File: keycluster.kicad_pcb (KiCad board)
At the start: 2 copper layers, 45.1 x 52.6 mm, 0 parts

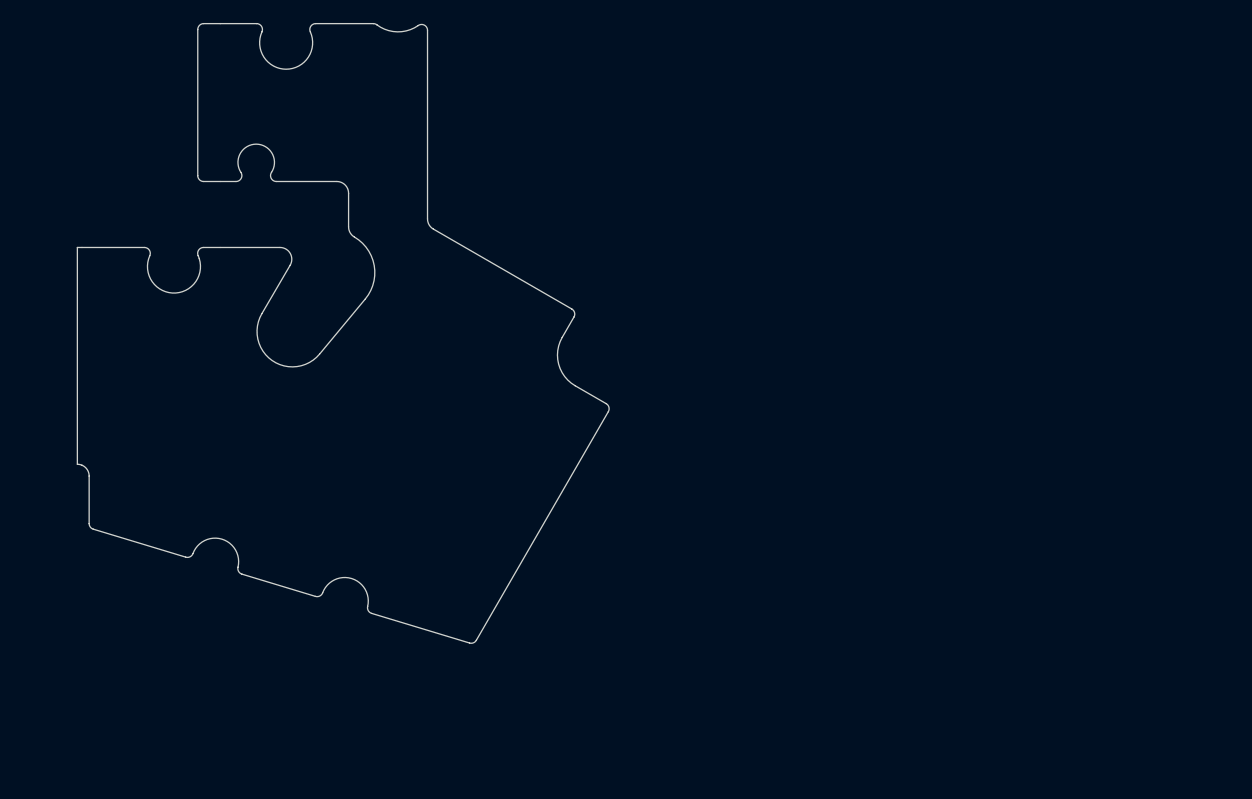
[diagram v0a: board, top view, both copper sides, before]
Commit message: Vertical and trackball pcb.
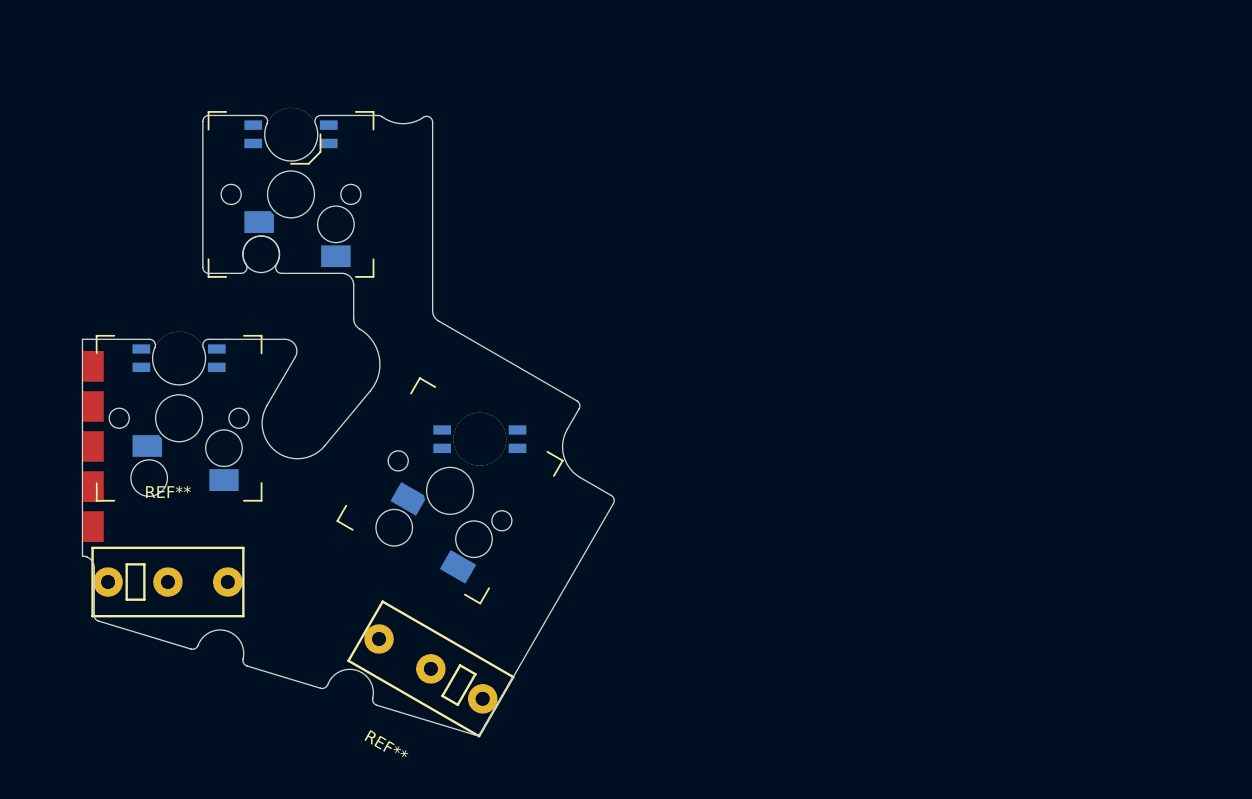
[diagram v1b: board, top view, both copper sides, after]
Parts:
- added REF**: CMI126603D08, ugl:CMI126603D08, F.Cu at (154.6, 128.0)
- added REF**: VAL**, ugl:RGB-LED-D, F.Cu at (158.7, 108.5)
- added REF**: VAL**, ugl:S01_Hybrid_Socket, F.Cu at (142.7, 87.7)
- added REF**: VAL**, ugl:S01_Hybrid_Socket, F.Cu at (133.2, 106.7)
- added REF**: VAL**, ugl:S01_Hybrid_Socket, F.Cu at (156.2, 112.9)
- added REF**: VAL**, ugl:RGB-LED-D, F.Cu at (133.2, 101.6)
- added REF**: VAL**, ugl:RGB_LED, F.Cu at (142.7, 82.6)
- added REF**: CMI126603D08, ugl:CMI126603D08, F.Cu at (132.3, 120.6)
- added REF**: VAL**, ugl:UHK_Connector_TrackBall_Pcb, F.Cu at (123.8, 100.0)

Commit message: Keycluster project files added.
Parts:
- removed REF** (x2): VAL**, ugl:RGB-LED-D
- removed REF** (x3): VAL**, ugl:S01_Hybrid_Socket
- removed REF**: VAL**, ugl:RGB_LED
- added C1: 0.47uF, UGL:SM0603, B.Cu at (154.0, 98.0)
- added C12: 1uF, UGL:SM0603, B.Cu at (138.7, 118.2)
- added C13: 10uF, UGL:SM1206_Diode, B.Cu at (150.8, 96.7)
- added C15: 0.1uF, UGL:SM0603, B.Cu at (157.5, 101.6)
- added C16: 0.47uF, UGL:SM0603, B.Cu at (159.6, 102.4)
- added C17: 0.1uF, UGL:SM0603, B.Cu at (155.5, 106.5)
- added C19: 0.47uF, UGL:SM0603, B.Cu at (153.5, 107.8)
- added C2: 1uF, UGL:SM0603, B.Cu at (138.2, 113.8)
- added C20: 0.1uF, UGL:SM0603, B.Cu at (150.4, 107.7)
- added C3: 0.1uF, UGL:SM0603, B.Cu at (161.0, 120.6)
- added C4: 0.1uF, UGL:SM0603, B.Cu at (141.1, 113.8)
- added C5: 0.1uF, UGL:SM0603, B.Cu at (152.8, 98.0)
- added C7: 0.1uF, UGL:SM0603, B.Cu at (133.7, 113.1)
- added C8: 0.1uF, UGL:SM0603, B.Cu at (135.0, 113.1)
- added D2: LED, UGL:SM0603_Diode, B.Cu at (150.5, 121.5)
- added D_LK1: RGB_LED, UGL:RGB_LED, F.Cu at (133.2, 101.6)
- added D_RK1: RGB_LED, UGL:RGB_LED, F.Cu at (158.7, 108.5)
- added D_TK1: ugl:RGB_LED, UGL:RGB_LED, F.Cu at (142.7, 82.6)
- added FB2: FERRITE_BEAD, UGL:SM0603, B.Cu at (134.5, 115.0)
- added P7: CONN_10, UGL:Tag_Connect_2x5_Header_With_Legs, B.Cu at (143.0, 123.7)
- added P9: CONN_5, FFC_Connector_51281-0594, F.Cu at (144.9, 111.8)
- added R1: 4.7K, UGL:SM0603, B.Cu at (159.8, 123.0)
- added R2: 330, UGL:SM0603, B.Cu at (150.5, 120.1)
- added R20: 100k, UGL:SM0603, B.Cu at (153.6, 110.8)
- added R3: 100K, UGL:SM0603, B.Cu at (149.2, 107.7)
- added R30: 100K, UGL:SM0603, B.Cu at (151.6, 107.7)
- added R6: 47, UGL:SM0603, B.Cu at (134.8, 122.7)
- added R7: 47, UGL:SM0603, B.Cu at (134.8, 118.6)
- added R8: 47K, UGL:SM0603, B.Cu at (157.5, 104.4)
- added SW1: CT05-3050-G1, UGL:Reed_Switch_CT05-3050-G1, B.Cu at (163.3, 122.0)
- added SW_LK1: LK, UGL:S01_Hybrid_Socket, F.Cu at (133.2, 106.7)
- added SW_RK1: RK, UGL:S01_Hybrid_Socket, F.Cu at (156.2, 112.9)
- added SW_TK1: TK, UGL:S01_Hybrid_Socket, F.Cu at (142.7, 87.7)
- added TP_3.3V1: 3.3V, UGL:Test_Point, B.Cu at (210.2, 104.6)
- added TP_5V1: 5V, UGL:Test_Point, B.Cu at (218.3, 101.9)
- added TP_CS1: LED_CS1, UGL:Test_Point, B.Cu at (148.4, 83.4)
- added TP_CS2: LED_CS2, UGL:Test_Point, B.Cu at (136.4, 104.6)
- added TP_CS3: LED_CS3, UGL:Test_Point, B.Cu at (162.0, 111.4)
- added TP_GND1: GND, UGL:Test_Point, B.Cu at (150.8, 93.1)
- added TP_IICRST1: IICRST, UGL:Test_Point, B.Cu at (218.8, 107.2)
- added TP_INTB1: SDA, UGL:Test_Point, B.Cu at (210.6, 106.7)
- added TP_KEY_LEFT1: KEYS_ROW2, UGL:Test_Point, B.Cu at (213.4, 99.9)
- added TP_KEY_MLEFT1: KEYS_ROW4, UGL:Test_Point, B.Cu at (220.0, 107.2)
- added TP_KEY_MRIGHT1: KEYS_ROW5, UGL:Test_Point, B.Cu at (221.7, 102.6)
- added TP_KEY_RIGHT1: KEYS_ROW3, UGL:Test_Point, B.Cu at (219.5, 100.7)
- added TP_KEY_TOP1: KEYS_ROW1, UGL:Test_Point, B.Cu at (213.3, 103.6)
- added TP_RESET1: RESET, UGL:Test_Point, B.Cu at (155.6, 121.3)
- added TP_SCL1: SCL, UGL:Test_Point, B.Cu at (216.4, 106.5)
- added TP_SCL_BOTTOM1: SCL_BOTTOM, UGL:Test_Point, B.Cu at (219.0, 110.1)
- added TP_SDA1: SDA, UGL:Test_Point, B.Cu at (212.6, 105.8)
- added TP_SDA_BOTTOM1: SDA_BOTTOM, UGL:Test_Point, B.Cu at (212.6, 108.2)
- added TP_SDB1: SDB, UGL:Test_Point, B.Cu at (206.8, 102.0)
- added TP_SW1: LED_SW1, UGL:Test_Point, B.Cu at (139.5, 85.8)
- added TP_SW2: LED_SW2, UGL:Test_Point, B.Cu at (137.8, 81.8)
- added TP_SW3: LED_SW3, UGL:Test_Point, B.Cu at (138.7, 100.8)
- added TP_SWDCLK1: SWDCLK, UGL:Test_Point, B.Cu at (207.0, 99.2)
- added TP_SWDIO1: SWDIO, UGL:Test_Point, B.Cu at (208.2, 99.2)
- added TP_TEST_LED1: TEST_LED, UGL:Test_Point, B.Cu at (217.8, 110.1)
- added TP_TEST_LED_R1: TEST_LED_R, UGL:Test_Point, B.Cu at (209.0, 104.6)
- added TP_VCC_BOTTOM1: VCC_BOTTOM, UGL:Test_Point, B.Cu at (210.4, 102.0)
- added U1: MKL03Z32VFK4, UGL:QFN-24-1EP_4x4mm_Pitch0.5mm, B.Cu at (145.0, 113.5)
- added U2: IS31FL3737, UGL:QFN-40_EP_5x5_Pitch0.4mm, B.Cu at (153.6, 102.6)
- added U4: ESD, UGL:SC-74-TVS, B.Cu at (131.0, 115.9)
- added VR1: MIC5504-3.3YM5, UGL:SOT-23-5, B.Cu at (138.2, 115.9)
- added hole 2.2mm: VAL**, UGL:hole_4.0mm, F.Cu at (144.8, 119.1)
- P2: renamed from REF**; value VAL** -> CONN_5
- SW_MLK1: renamed from REF**; value CMI126603D08 -> MLK
- SW_MRK1: renamed from REF**; value CMI126603D08 -> MRK
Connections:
- P2 pad 1: (no net) -> /VCC_BOTTOM
- P2 pad 2: (no net) -> /SDA_BOTTOM
- P2 pad 3: (no net) -> /SCL_BOTTOM
- P2 pad 4: (no net) -> GND
- P2 pad 5: (no net) -> GND
- SW_MLK1 pad 1: (no net) -> /KEY_MLEFT
- SW_MLK1 pad 2: (no net) -> GND
- SW_MRK1 pad 1: (no net) -> /KEY_MRIGHT
- SW_MRK1 pad 2: (no net) -> GND

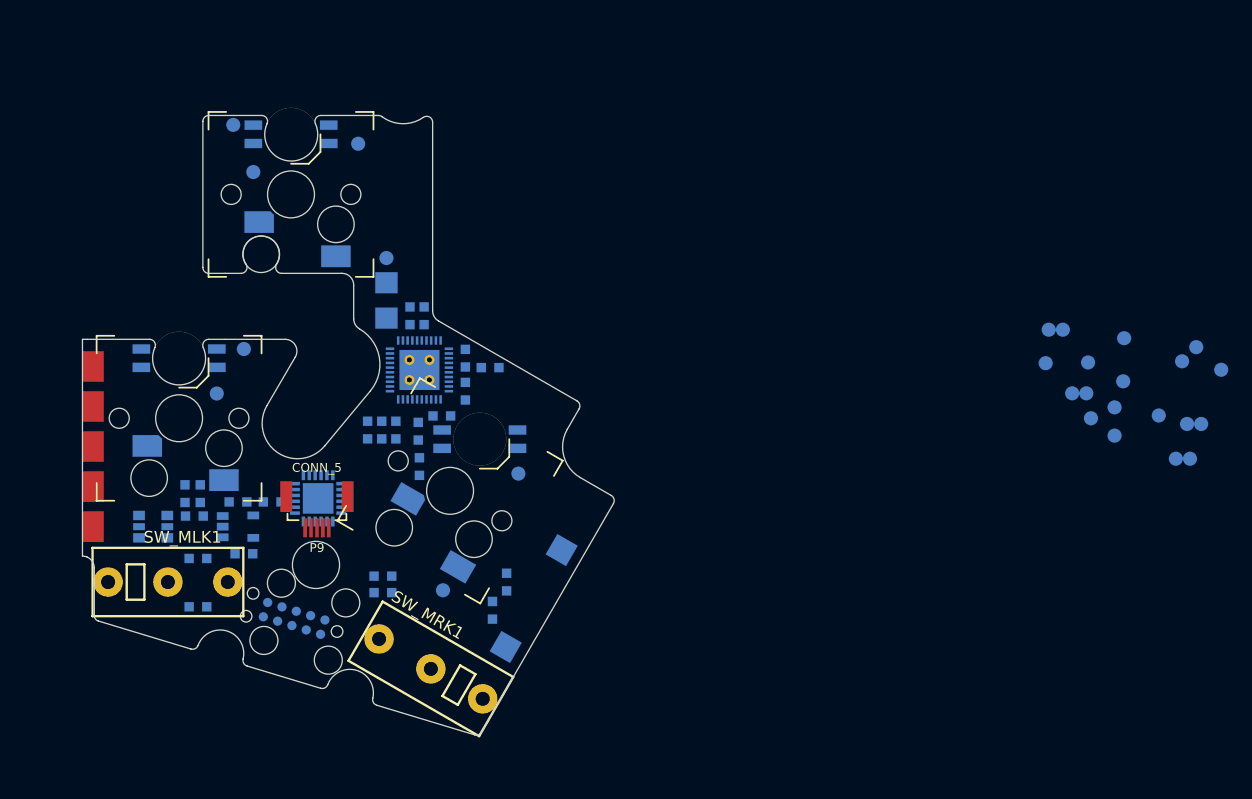
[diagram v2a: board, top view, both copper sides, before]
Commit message: Wiring on main pcb.
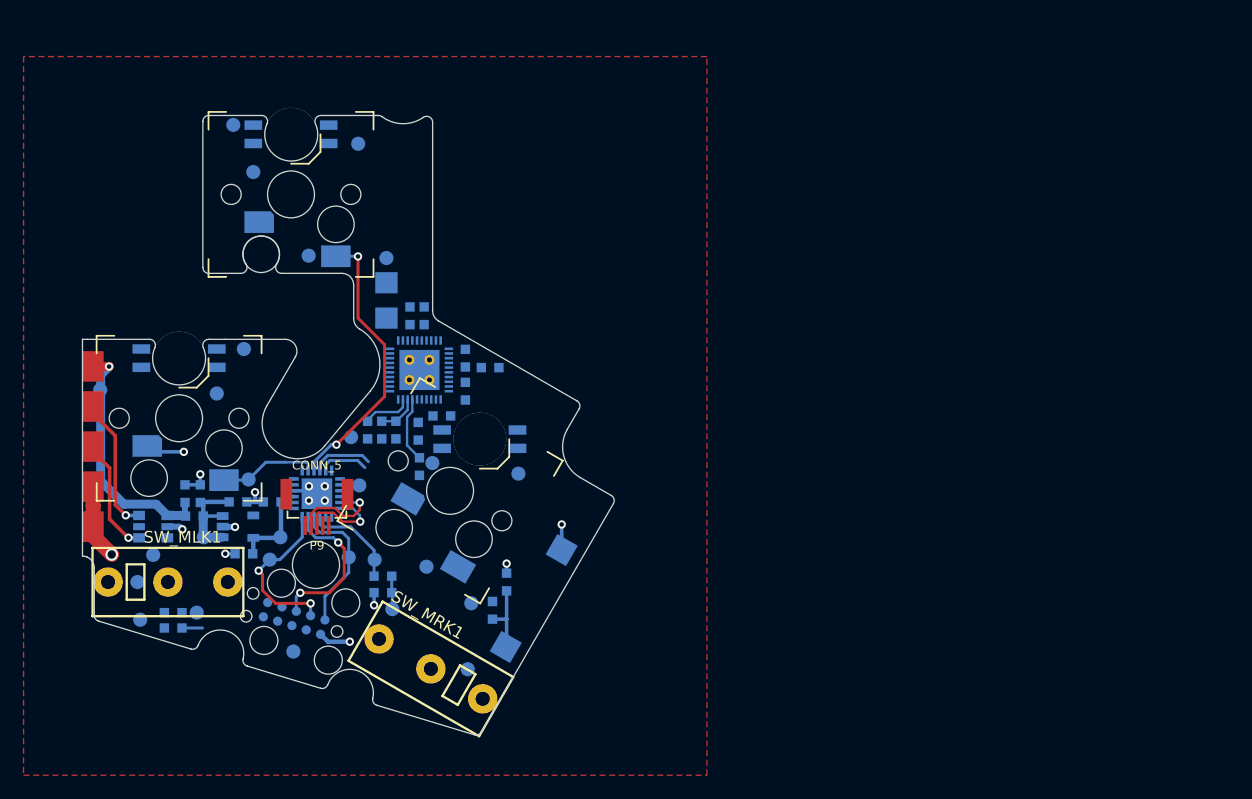
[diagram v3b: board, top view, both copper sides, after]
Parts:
- moved TP_KEY_MLEFT1 91.3 mm to (129.7, 120.6)
- moved TP_SCL_BOTTOM1 90.1 mm to (129.9, 123.8)
- moved TP_5V1 84.4 mm to (135.3, 116.8)
- moved TP_VCC_BOTTOM1 83.9 mm to (126.5, 104.3)
- moved TP_SDA_BOTTOM1 82.2 mm to (131.0, 118.3)
- moved TP_SDA1 79.8 mm to (134.7, 123.2)
- moved TP_SCL1 76.1 mm to (142.9, 126.5)
- moved TP_KEY_LEFT1 75.3 mm to (139.1, 111.9)
- moved TP_IICRST1 70.4 mm to (148.5, 112.4)
- moved TP_SWDIO1 70.1 mm to (140.9, 118.7)
- moved TP_KEY_TOP1 70.0 mm to (144.2, 92.9)
- moved TP_3.3V1 69.5 mm to (141.8, 116.8)
- moved TP_KEY_MRIGHT1 68.8 mm to (157.7, 128.0)
- moved TP_TEST_LED1 68.5 mm to (149.8, 118.7)
- moved TP_KEY_RIGHT1 67.9 mm to (154.2, 119.3)
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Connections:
- U1 pad 10: /KEY_MLEFT -> /KEY_RIGHT
- U1 pad 7: /KEY_TOP -> /KEY_MLEFT
- U1 pad 9: /KEY_RIGHT -> /KEY_TOP
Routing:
- net GND: track 0.00 -> 25.7 mm, vias 0 -> 15
- net /KEY_TOP: track 0.00 -> 23.7 mm, vias 0 -> 2
- net /VCC_BOTTOM: track 0.00 -> 20.9 mm, vias 0 -> 1
- net /RESET: track 0.00 -> 19.3 mm, vias 0 -> 2
- net /SWDIO: track 0.00 -> 14.0 mm, vias 0 -> 2
- net /SWDCLK: track 0.00 -> 11.9 mm
- net /SDA_BOTTOM: track 0.00 -> 11.5 mm, vias 0 -> 1
- net /SCL: track 0.00 -> 10.1 mm, vias 0 -> 1
- net /SCL_BOTTOM: track 0.00 -> 9.90 mm, vias 0 -> 1
- net +5V: track 0.00 -> 8.64 mm
- net /KEY_LEFT: track 0.00 -> 8.39 mm
- net /TEST_LED: track 0.00 -> 8.34 mm
- net +3V3: track 0.00 -> 7.98 mm
- net /ADDR: track 0.00 -> 7.67 mm, vias 0 -> 1
- net /INTB: track 0.00 -> 5.57 mm
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- added copper zone on F.Cu, net GND
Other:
- net class Default: clearance 0.2 -> 0.1778; trace_width 0.25 -> 0.2032; via_dia 0.8 -> 1.0668; via_drill 0.4 -> 0.7112
- rule trace_clearance: 0.2 -> 0.1778
- rule trace_min: 0.2 -> 0.2032
- rule via_min_drill: 0.3 -> 0.381
- rule via_min_size: 0.4 -> 0.7112

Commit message: Wiring on main pcb.
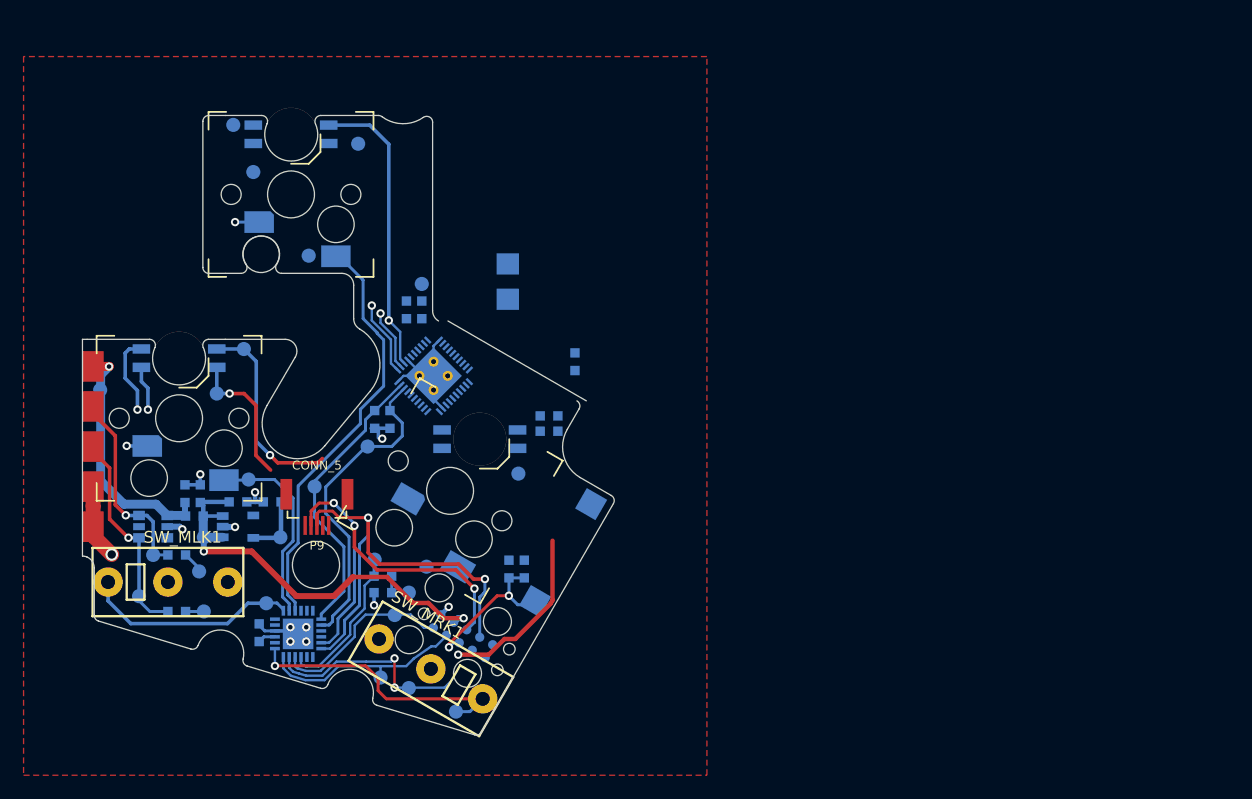
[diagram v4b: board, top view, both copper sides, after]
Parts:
- removed C1: 0.47uF, UGL:SM0603
- removed C20, C5: 0.1uF, UGL:SM0603
- removed R20: 100k, UGL:SM0603
- removed TP_INTB1: SDA, UGL:Test_Point
- moved P7 14.4 mm to (157.3, 125.2), turned to 330 degrees
- moved TP_SWDIO1 13.7 mm to (150.3, 128.7)
- moved U1 12.0 mm to (143.3, 125.0)
- moved C19 11.1 mm to (164.6, 107.8), turned to 0 degrees
- moved TP_KEY_MLEFT1 11.1 mm to (140.6, 122.4)
- moved C13 10.4 mm to (161.1, 95.1)
- moved R8 9.63 mm to (166.8, 101.9)
- moved C17 9.49 mm to (152.5, 97.5), turned to 90 degrees
- moved TP_RESET1 8.94 mm to (152.7, 129.6)
- moved TP_SCL1 8.33 mm to (135.3, 123.1)
- moved C12 6.82 mm to (140.0, 124.9), turned to 270 degrees
- moved C16 6.47 mm to (164.6, 106.5)
- moved TP_SWDCLK1 6.26 mm to (151.5, 123.4)
- moved C15 5.52 mm to (153.8, 97.5)
- moved R6 4.91 mm to (133.0, 118.3)
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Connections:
- U1 pad 1: Net-(U1-Pad1) -> /KEY_MRIGHT
- U1 pad 11: /KEY_MRIGHT -> Net-(U1-Pad11)
- U1 pad 13: /SDB -> /IICRST
- U1 pad 14: /IICRST -> /SDB
- U2 pad 37: /INTB -> Net-(U2-Pad37)
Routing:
- net /LED_SW3: track 0.00 -> 42.0 mm, vias 0 -> 2
- net /ADDR: track 7.67 -> 40.7 mm, vias 1 -> 2
- net +5V: track 8.64 -> 36.6 mm, vias 0 -> 2
- net /SCL: track 10.1 -> 36.3 mm, vias 1 -> 3
- net /SDB: track 3.49 -> 27.2 mm
- net /IICRST: track 4.21 -> 24.8 mm
- net /KEY_MRIGHT: track 4.22 -> 23.6 mm, vias 0 -> 1
- net /KEY_MLEFT: track 0.00 -> 18.3 mm
- net +3V3: track 7.98 -> 23.3 mm, vias 0 -> 1
- net /RESET: track 19.3 -> 31.8 mm, vias 2 -> 4
- net /LED_CS2: track 0.00 -> 12.0 mm, vias 0 -> 1
- net /LED_SW2: track 0.00 -> 11.9 mm, vias 0 -> 2
- net /KEY_TOP: track 23.7 -> 35.6 mm, vias 2 -> 0
- net /LED_SW1: track 0.00 -> 10.2 mm, vias 0 -> 2
- net /KEY_LEFT: track 8.39 -> 16.6 mm
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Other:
- outline, holes or cut-outs redrawn
